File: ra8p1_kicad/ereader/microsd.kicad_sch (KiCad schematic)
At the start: 4 parts, among them J2 DM3AT-SF-PEJM5

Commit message: hardware: integrate supervised microSD power and SDHI bus (#827, #845, #846)
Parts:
- added C102: 10u, symbol Device:C
- added C103: 22u, symbol Device:C
- added C104, C105, C106, C107, C48, C97, C98: 100n, symbol Device:C_Small
- added D10, D11, D12, D7, D8, D9: ESD441DPYR, symbol Device:D_Zener
- added R76: 2.21k, symbol Device:R
- added R77, R78, R79, R80, R81: 10k, symbol Device:R
- added R82: 330, symbol Device:R
- added R83, R84, R85, R86, R87, R88: 33, symbol Device:R
- added R89, R90, R91, R92, R93: 47k, symbol Device:R
- added U17: TPS22950CDDCR, symbol Power_Devices:TPS22950CDDCR
- added U18: TPS3808G30DBVR, symbol Power_Devices:TPS3808G30DBVR
- added U19, U20: SN74LVC1G97DBVR, symbol Power_Devices:SN74LVC1G97DBVR
- added U21, U22: TMUX1511RSVR, symbol Power_Devices:TMUX1511RSVR
- D6: Procurement_Status Selected reuse candidate for mechanical CD; wetting, bounce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 -> Selected for mechanical card detect; native SD power/data i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; Selection_Basis CMS-012: TI SLVSH26B section 5.6 <100nA over +/-5.5V across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 -> CMS-012: TI SLVSH26C sections 5.4/5.6: recommended VIO 0..5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; Sourcing_Snapshot 2026-09-07: DigiKey stock 3273; USD 0.34/0.207/0.1291 at 1/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 -> 2026-09-12 DigiKey: Active; 2456 in stock; USD 0.34/0.207/0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
- J2: Procurement_Status Active socket; pin map verified CMS-003; circuit integratio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 -> Active socket; CMS-003 pin map verified; native SD power/da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
- R72, R73: Procurement_Status Selected reuse candidate for mechanical CD; wetting, bounce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 -> Selected for mechanical card detect; native SD power/data i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
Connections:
- net +3V3_MCU: now also C102.1, C105.1, C106.1, C107.1, C48.1, C97.1, C98.1, R81.1, U17.2 (VIN), U18.6 (VDD), U19.5 (VCC), U20.5 (VCC), U21.16 (VDD), U22.16 (VDD)
- net GND: now also C102.2, C103.2, C104.2, C105.2, C106.2, C107.2, C48.2, C97.2, C98.2, D10.2 (A), D11.2 (A), D12.2 (A), D7.2 (A), D8.2 (A), D9.2 (A), R76.2, R77.2, R78.2, R79.2, R80.2, R82.2, U17.3 (GND), U18.2 (GND), U19.1 (IN1), U19.2 (GND), U20.1 (IN1), U20.2 (GND), U21.8 (GND), U22.11, U22.15, U22.8 (GND)
- net at J2.1 (DAT2): now also D9.1 (K), R91.2, U22.3
- net at J2.2 (DAT3): now also D10.1 (K), R92.2, U22.6
- net at J2.3 (CMD): now also D11.1 (K), R93.2, U21.6
- net VDD_SD: now reaches J2.4 (VDD)
- net VDD_SD: now also C103.1, C104.1, R82.1, R89.1, R90.1, R91.1, R92.1, R93.1, U17.5 (VOUT), U18.5 (SENSE)
- net at J2.5 (CLK): now also D12.1 (K), U21.3
- net at J2.7 (DAT0): now also D7.1 (K), R89.2, U21.9
- net at J2.8 (DAT1): now also D8.1 (K), R90.2, U21.13
- new net: R84.2, U21.5
- new net: R76.1, U17.4 (ILIM)
- new net: R85.2, U22.5
- new net: R87.2, U21.14
- new net: R86.2, U22.2
- new net: R83.2, U21.2
- new net: R88.2, U21.10
- new net MCU_RESET_N: U19.6 (IN2)
- new net SD_CLK: R83.1
- new net SD_CMD: R84.1
- new net SD_DAT0: R88.1
- new net SD_DAT1: R87.1
- new net SD_DAT2: R86.1
- new net SD_DAT3: R85.1
- new net SD_IO_EN: R80.1, U20.4 (Y), U21.1, U21.11, U21.15, U21.4, U22.1, U22.4
- new net SD_IO_REQ: R79.1, U20.3 (IN0)
- new net SD_PWR_ON: R77.1, U17.1 (ON), U18.3 (~{MR}), U19.4 (Y)
- new net SD_PWR_REQ: R78.1, U19.3 (IN0)
- new net SD_READY: R81.2, U17.6 (~{FLT}), U18.1 (~{RESET}), U20.6 (IN2)
- no-connect marks 0 -> 5
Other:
- note added: "SD-001 | POWER / READY / GATES U17 ILIM: R76=2.21k; TI row .38/.50/.62A min/typ/max. Card+support=.270A; Vmin=3.151820-.270*(.116+.100) =3.093500V > G30 rise screen 2.902647V; CT open 12..28ms. FLT reports thermal/reverse, not current limiting alone. U19 ANDs request/reset; U20 ANDs IO request/READY. ON-low load<=3.6/70k+.1/9801+12uA=73.632uA<100uA. Gate VOL<=.1V (VCC 1.65..5.5V) < ON VIL .35V. C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"
- note added: "SD-002 | DISCHARGE / ISOLATION R82=330R; Rmax=330*1.01*1.02; Cisland<=40.4865uF. Require cutoff+isolation<=10ms and total return<=20uA. Vinf=20uA*Rmax; t=.010+Rmax*C*ln((3.6-Vinf)/(.3-Vinf)) =44.491861ms; require >=50ms before repowering. IO request OFF; wait>=1us at valid main; then power OFF. No reliance on QOD at zero VIN. Capacitance/return bounds require measurement; no arbitrary-fault or da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"
- note added: "SD-003 | MAIN LOAD / RESET FANOUT Main=.750+.505+.250+.250+.050+.250+.020=2.075A. 2.070A only if existing 50mA already includes radio 5mA. At Vin 3.2V / assumed 75% efficiency / Vout 3.393012V: Iin=2.933542A; converter loss=2.346834W; thermal/source OPEN. SD adds 10.6uF main and 22.1uF switched, plus card. RST-002: U19 adds 5uA; devices 17uA+overhead 13uA=30uA. Reset sink=.376190mA<.4mA; high>=2.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"

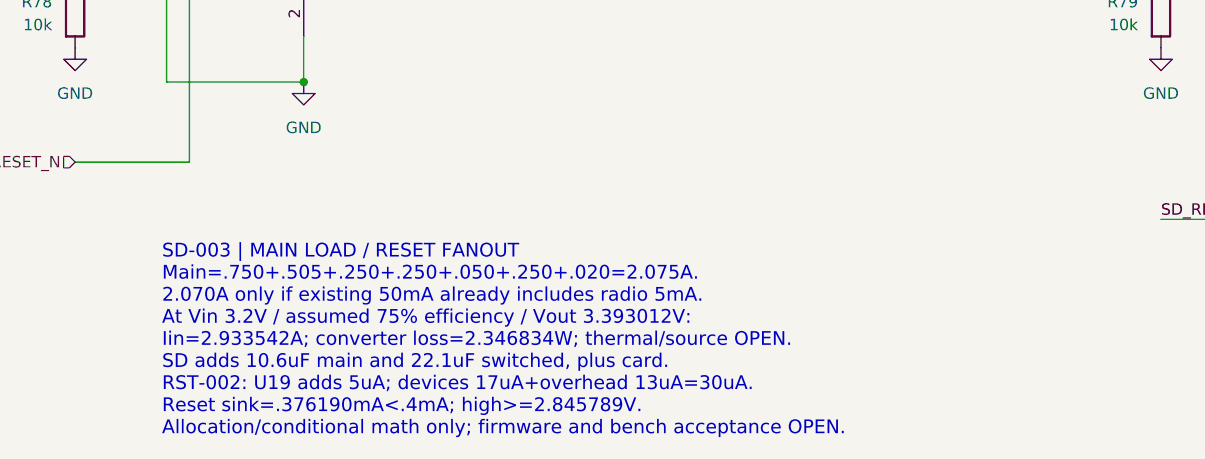
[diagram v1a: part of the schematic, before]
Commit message: hardware: integrate MIPI host 1.8V supply and bypass (#824, #841)
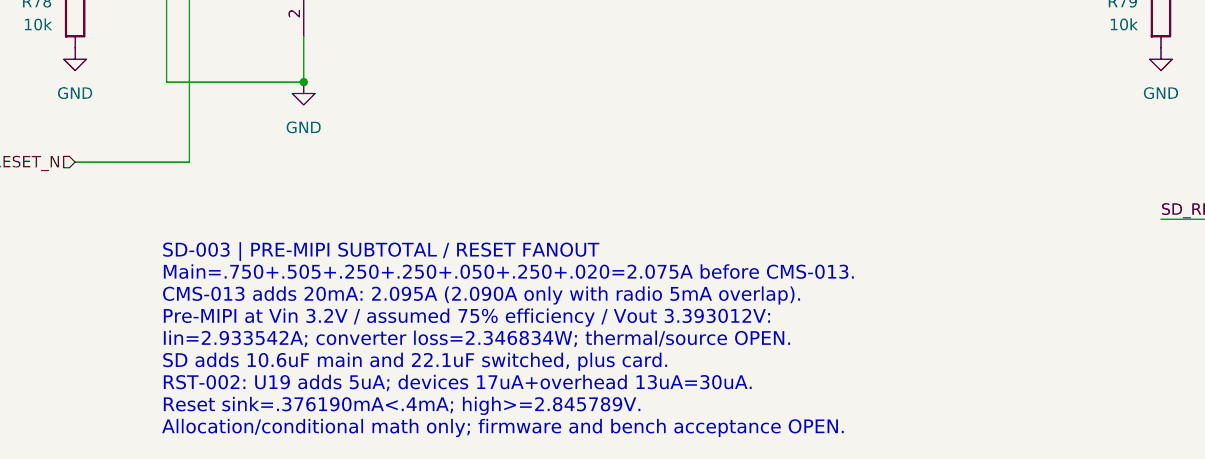
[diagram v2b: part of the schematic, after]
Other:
- note added: "SD-003 | PRE-MIPI SUBTOTAL / RESET FANOUT Main=.750+.505+.250+.250+.050+.250+.020=2.075A before CMS-013. CMS-013 adds 20mA: 2.095A (2.090A only with radio 5mA overlap). Pre-MIPI at Vin 3.2V / assumed 75% efficiency / Vout 3.393012V: Iin=2.933542A; converter loss=2.346834W; thermal/source OPEN. SD adds 10.6uF main and 22.1uF switched, plus card. RST-002: U19 adds 5uA; devices 17uA+overhead 13uA=30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"
- note removed: "SD-003 | MAIN LOAD / RESET FANOUT Main=.750+.505+.250+.250+.050+.250+.020=2.075A. 2.070A only if existing 50mA already includes radio 5mA. At Vin 3.2V / assumed 75% efficiency / Vout 3.393012V: Iin=2.933542A; converter loss=2.346834W; thermal/source OPEN. SD adds 10.6uF main and 22.1uF switched, plus card. RST-002: U19 adds 5uA; devices 17uA+overhead 13uA=30uA. Reset sink=.376190mA<.4mA; high>=2.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"
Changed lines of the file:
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@@
 		)
 	)
-	(text "SD-003 | MAIN LOAD / RESET FANOUT\nMain=.750+.505+.250+.250+.050+.250+.020=2.075A.\n2.070A only if existing 50mA already includes radio 5mA.\nAt Vin 3.2V / assumed 75% efficiency / Vout 3.393012V:\nIin=2.933542A; converter loss=2.346834W; thermal/source OPEN.\nSD adds 10.6uF main and 22.1uF switched, plus card.\nRST-002: U19 adds 5uA; devices 17uA+overhead 13uA=30uA.\nReset sink=.376190mA<.4mA; high>=2.845789V.\nAllocation/conditional math only; firmware and bench acceptance OPEN."
+	(text "SD-003 | PRE-MIPI SUBTOTAL / RESET FANOUT\nMain=.750+.505+.250+.250+.050+.250+.020=2.075A before CMS-013.\nCMS-013 adds 20mA: 2.095A (2.090A only with radio 5mA overlap).\nPre-MIPI at Vin 3.2V / assumed 75% efficiency / Vout 3.393012V:\nIin=2.933542A; converter loss=2.346834W; thermal/source OPEN.\nSD adds 10.6uF main and 22.1uF switched, plus card.\nRST-002: U19 adds 5uA; devices 17uA+overhead 13uA=30uA.\nReset sink=.376190mA<.4mA; high>=2.845789V.\nAllocation/conditional math only; firmware and bench acceptance OPEN."
 		(exclude_from_sim no)
 		(at 38.862 260.604 0)

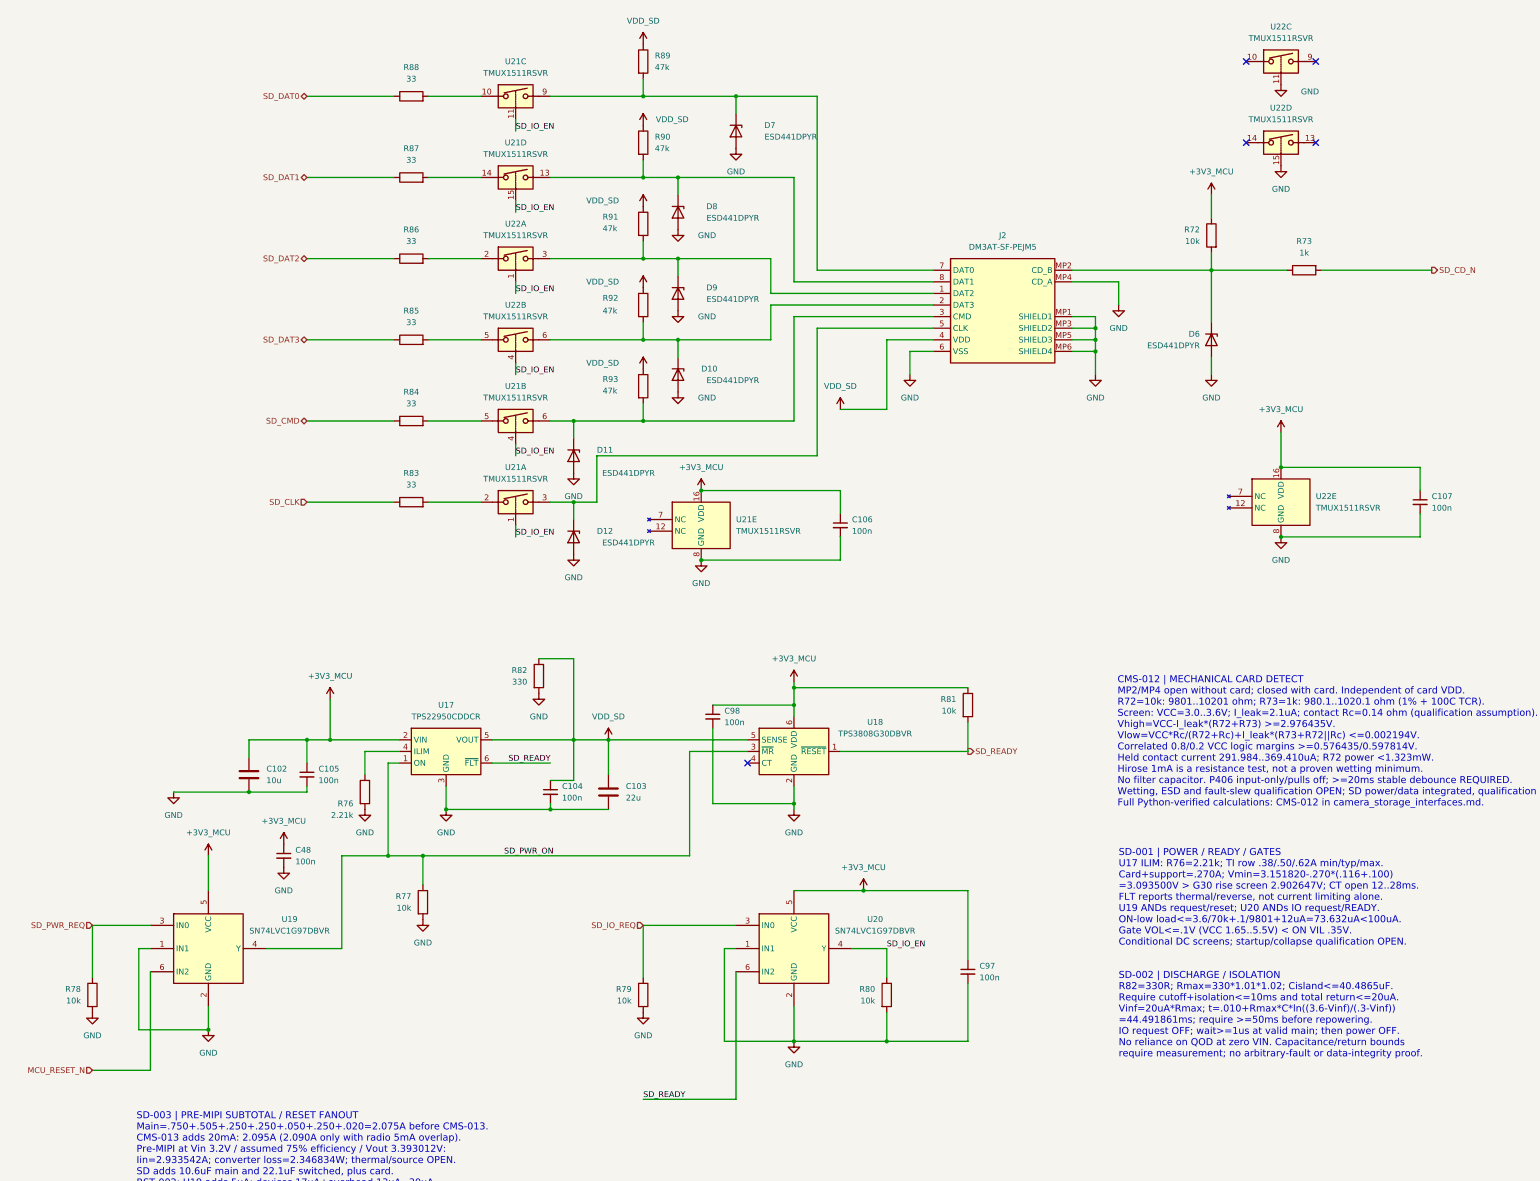
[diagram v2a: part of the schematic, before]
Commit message: wip(hardware): preserve schematic cleanup and CEU host ports
Checkpoint cosmetic cleanup across the schematic hierarchy and eleven parallel-camera host ports. Refresh the complete 13-page PDF. All 334 existing net partitions and 271 component records match the prior CEU checkpoint; all 128 ERC identities remain unchanged. Electrical design is incomplete; this is a WIP checkpoint for #821 and #841.
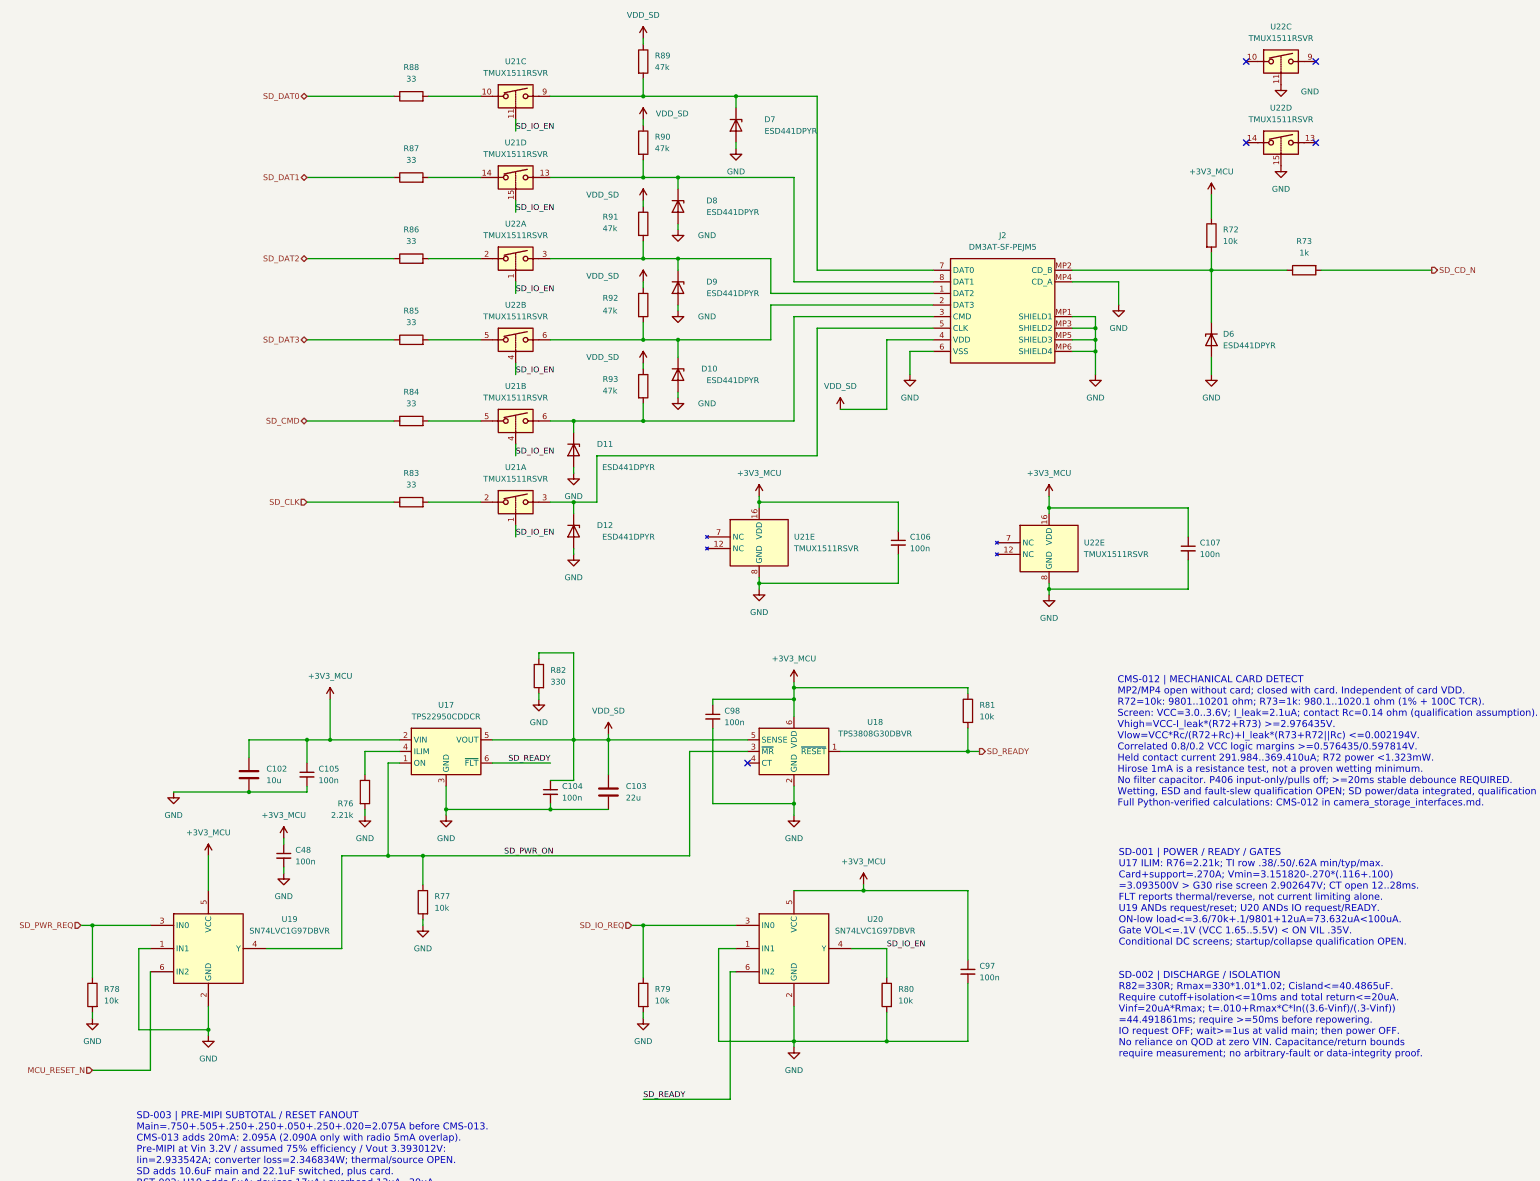
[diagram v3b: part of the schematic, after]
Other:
- moved on the sheet: C106, C107, D11, D12, D6, D7, D8, D9, R81, U21E, U22E
